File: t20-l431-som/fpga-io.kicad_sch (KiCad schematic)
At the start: 2 parts, among them U2 T20W80, U4 MODULE_INTERNAL_T20_L431_HOST

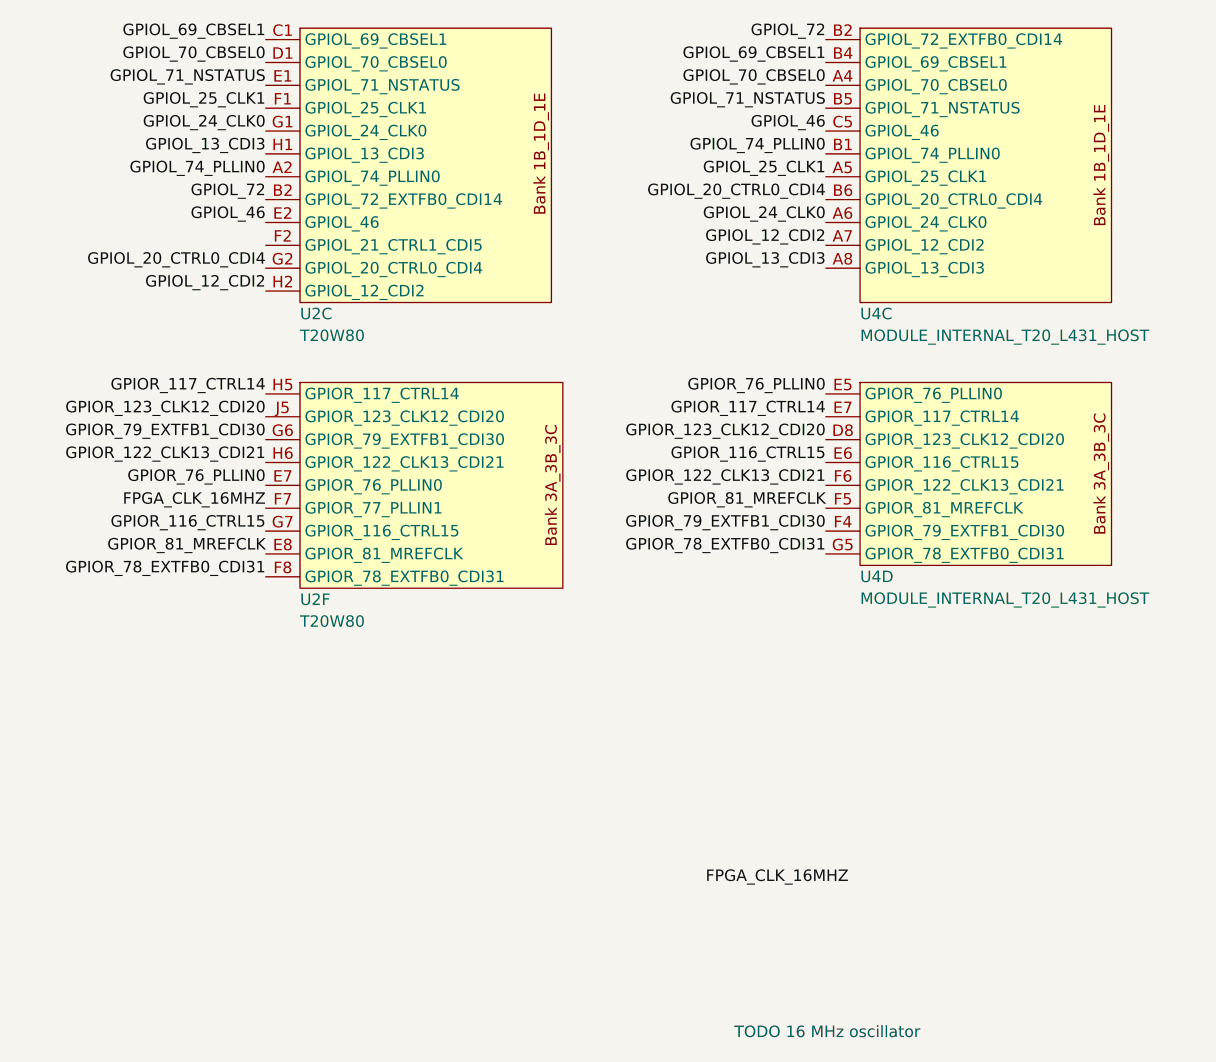
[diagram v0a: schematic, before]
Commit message: Continued STM32 fanout
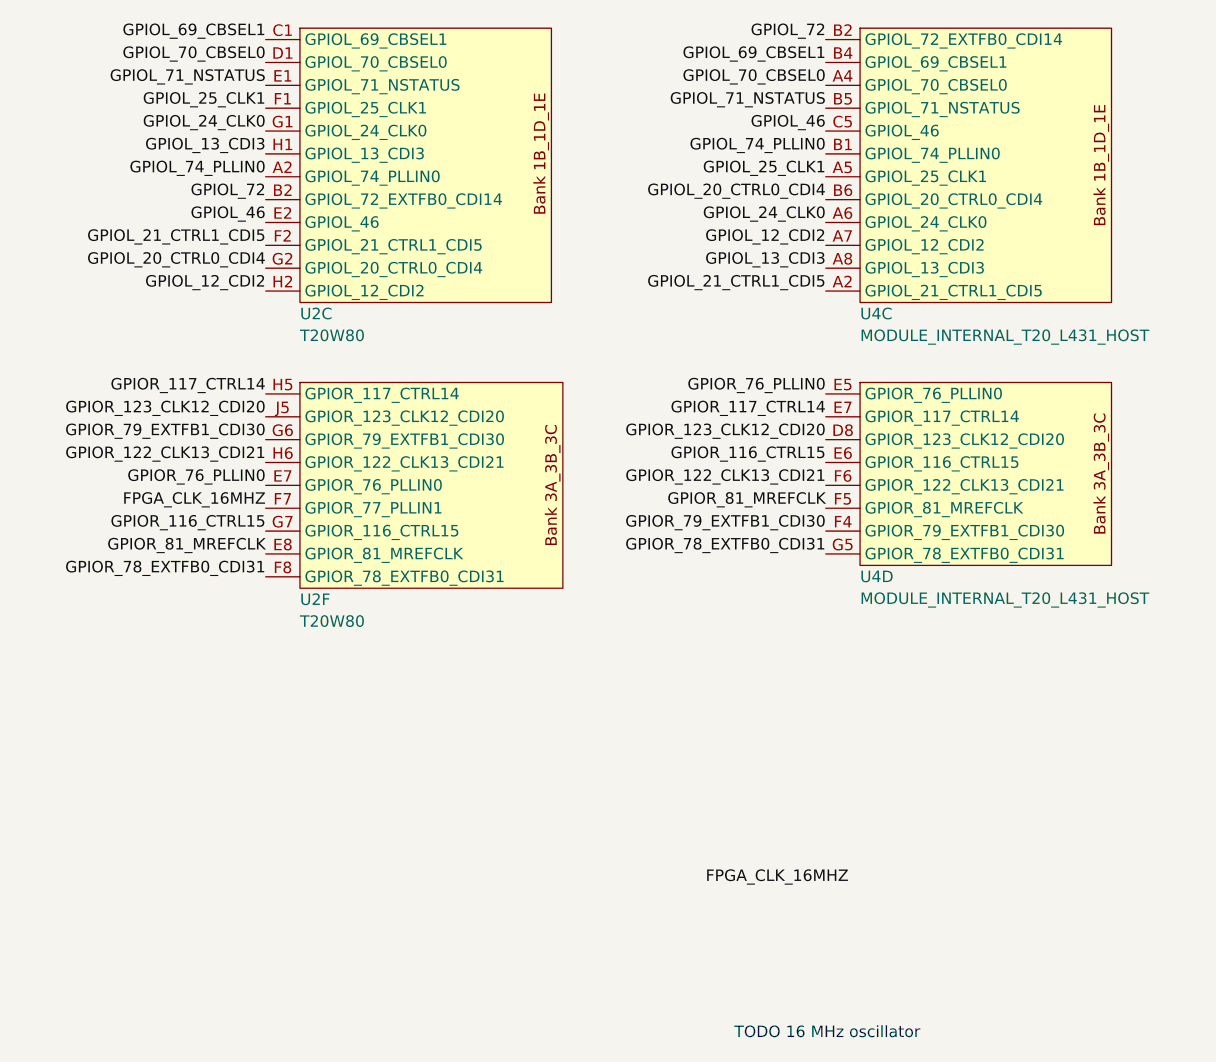
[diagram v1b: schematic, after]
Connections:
- net GPIOL_21_CTRL1_CDI5: now reaches U2.F2 (GPIOL_21_CTRL1_CDI5)
- net GPIOL_21_CTRL1_CDI5: now also U4.A2 (GPIOL_21_CTRL1_CDI5)
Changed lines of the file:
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@@
+		)
+	)
+	(label "GPIOL_21_CTRL1_CDI5"
+		(at 40.64 45.72 180)
+		(effects
+			(font
+				(size 1.27 1.27)
+			)
+			(justify right bottom)
 		)
 	)
@@
 	(label "GPIOR_78_EXTFB0_CDI31"
 		(at 102.87 80.01 180)
+		(effects
+			(font
+				(size 1.27 1.27)
+			)
+			(justify right bottom)
+		)
+	)
+	(label "GPIOL_21_CTRL1_CDI5"
+		(at 102.87 50.8 180)
 		(effects
 			(font
@@
 		)
 		(pin "G2"
+		)
+		(pin "E1"
+		)
+		(pin "F1"
+		)
+		(pin "D1"
+		)
+		(pin "C1"
+		)
+		(pin "F3"
+		)
+		(pin "A2"
+		)
+		(pin "A1"
+		)
+		(pin "K2"
+		)
+		(pin "P1"
+		)
+		(pin "N1"
+		)
+		(pin "M2"
+		)
+		(pin "M1"
+		)
+		(pin "R1"
+		)
+		(pin "N2"
+		)
+		(pin "P2"
+		)
+		(pin "R2"
+		)
+		(pin "R3"
+		)
+		(pin "P4"
+		)
+		(pin "P3"
 		)
 		(instances
@@
 		(pin "G1"
 		)
+		(pin "E1"
+		)
+		(pin "F1"
+		)
+		(pin "D1"
+		)
+		(pin "A2"
+		)
+		(pin "C1"
+		)
+		(pin "F3"
+		)
+		(pin "P3"
+		)
+		(pin "A1"
+		)
+		(pin "M1"
+		)
+		(pin "P1"
+		)
+		(pin "N1"
+		)
+		(pin "M2"
+		)
+		(pin "K2"
+		)
+		(pin "R1"
+		)
+		(pin "N2"
+		)
+		(pin "P2"
+		)
+		(pin "R2"
+		)
+		(pin "R3"
+		)
+		(pin "P4"
+		)
 		(instances

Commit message: Added oscillator
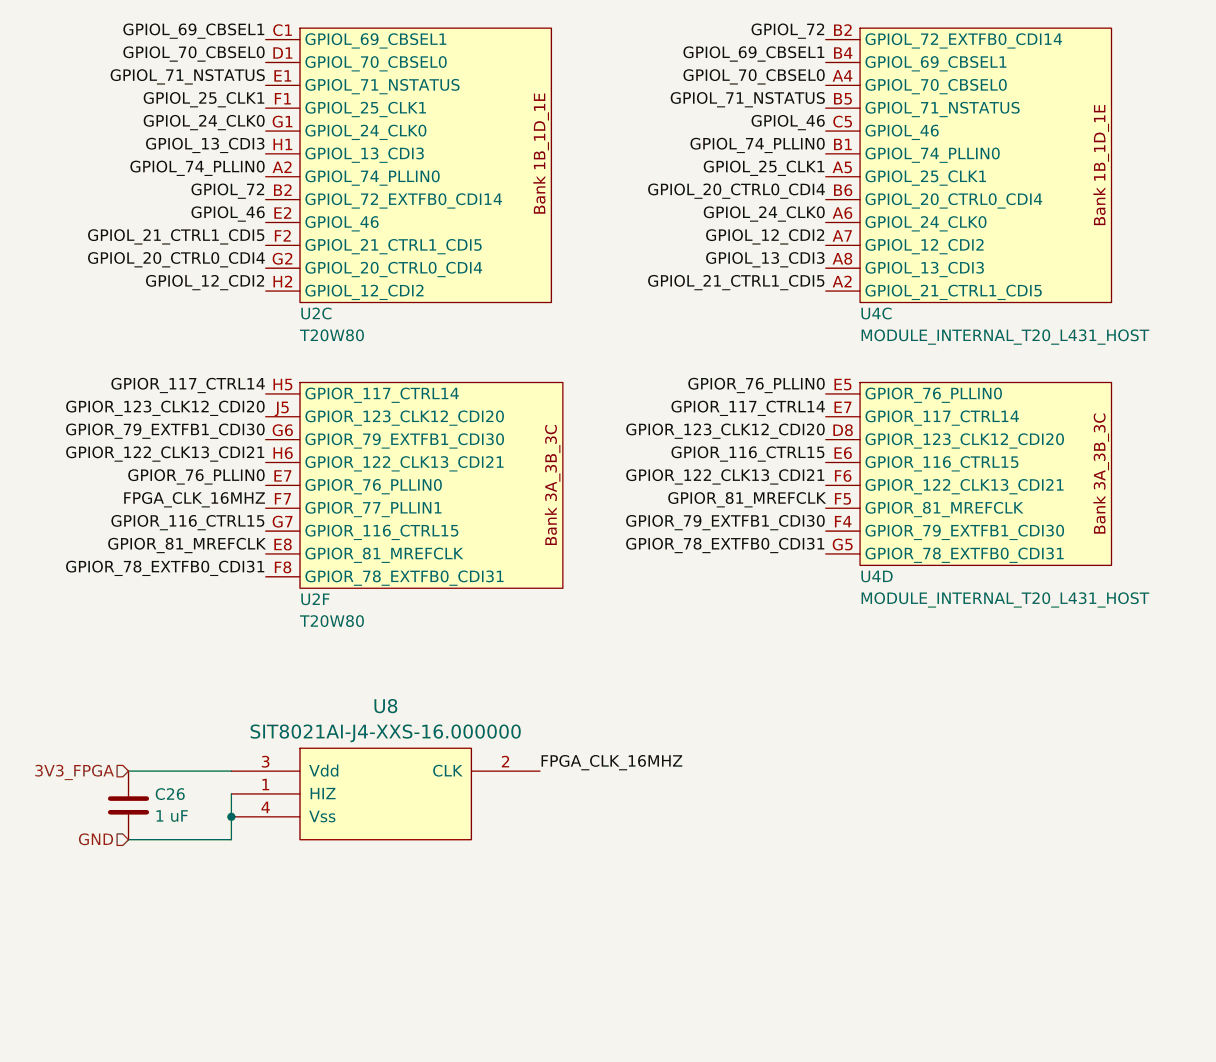
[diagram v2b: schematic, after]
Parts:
- added C26: 1 uF, azonenberg_pcb:EIA_0201_CAP_NOSILK, symbol device:C
- added U8: SIT8021AI-J4-XXS-16.000000, azonenberg_pcb:OSCILLATOR_SIT8021_WLCSP, symbol osc-azonenberg:SIT8021_WLCSP
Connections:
- net FPGA_CLK_16MHZ: now also U8.2 (CLK)
- new net 3V3_FPGA: C26.1, U8.3 (Vdd)
- new net GND: C26.2, U8.1 (HIZ), U8.4 (Vss)
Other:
- note removed: "TODO 16 MHz oscillator"
